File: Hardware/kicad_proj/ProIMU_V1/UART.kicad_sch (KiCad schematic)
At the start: 5 parts

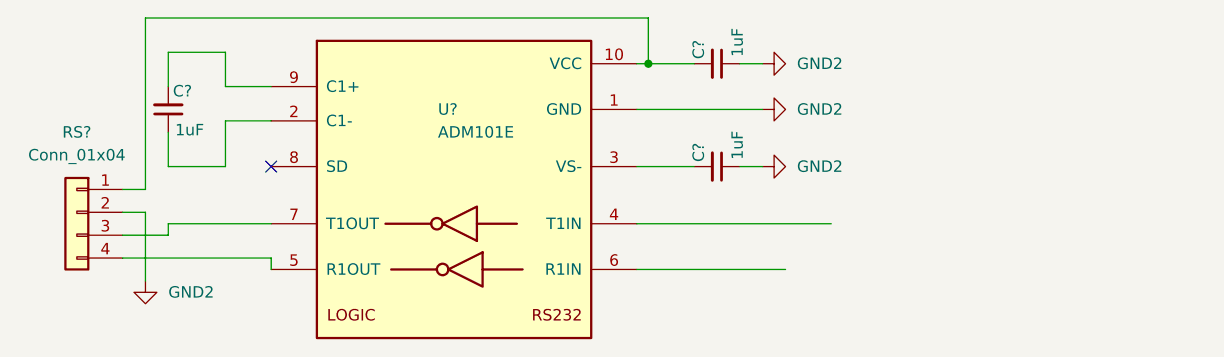
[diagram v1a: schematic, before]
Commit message: Updated schematic and removed redundant schematic
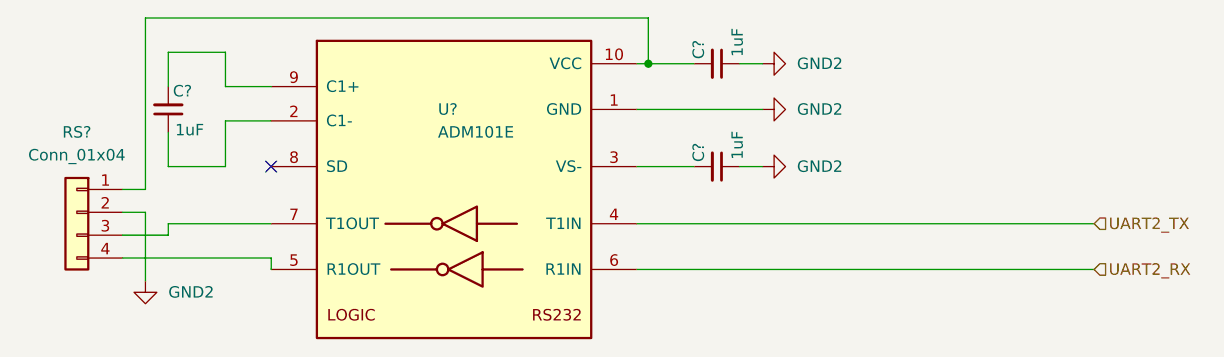
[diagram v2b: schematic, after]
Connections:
- net UART2_TX: now reaches U?.4 (T1IN)
- net UART2_RX: now reaches U?.6 (R1IN)
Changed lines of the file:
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@@
     (stroke (width 0) (type default) (color 0 0 0 0))
   )
-  (wire (pts (xy 168.91 99.06) (xy 190.5 99.06))
+  (wire (pts (xy 168.91 99.06) (xy 219.71 99.06))
     (stroke (width 0) (type default) (color 0 0 0 0))
   )
@@
     (stroke (width 0) (type default) (color 0 0 0 0))
   )
-  (wire (pts (xy 168.91 104.14) (xy 185.42 104.14))
+  (wire (pts (xy 168.91 104.14) (xy 219.71 104.14))
     (stroke (width 0) (type default) (color 0 0 0 0))
   )
@@
     (stroke (width 0) (type default) (color 0 0 0 0))
   )
+  (hierarchical_label "UART2_RX" (shape input) (at 219.71 104.14 0)
+    (effects (font (size 1.27 1.27)) (justify left))
+  )
+  (hierarchical_label "UART2_TX" (shape input) (at 219.71 99.06 0)
+    (effects (font (size 1.27 1.27)) (justify left))
+  )
   (symbol (lib_id "power:GND2") (at 182.88 86.36 90) (unit 1)

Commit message: Updated Schematic and Layout
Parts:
- gave numbers to parts that had none: 5
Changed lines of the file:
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@@
   (symbol (lib_id "power:GND2") (at 182.88 86.36 90) (unit 1)
     (in_bom yes) (on_board yes) (fields_autoplaced)
-    (property "Reference" "#PWR?" (id 0) (at 189.23 86.36 0)
+    (property "Reference" "#PWR0119" (id 0) (at 189.23 86.36 0)
       (effects (font (size 1.27 1.27)) hide)
     )
@@
   (symbol (lib_id "Device:C_Small") (at 177.8 81.28 270) (unit 1)
     (in_bom yes) (on_board yes)
-    (property "Reference" "C?" (id 0) (at 175.768 80.772 0)
+    (property "Reference" "C7" (id 0) (at 175.768 80.772 0)
       (effects (font (size 1.27 1.27)) (justify right))
     )
@@
   (symbol (lib_id "Device:C_Small") (at 116.84 86.36 180) (unit 1)
     (in_bom yes) (on_board yes)
-    (property "Reference" "C?" (id 0) (at 117.348 84.328 0)
+    (property "Reference" "C6" (id 0) (at 117.348 84.328 0)
       (effects (font (size 1.27 1.27)) (justify right))
     )
@@
   (symbol (lib_id "Connector_Generic:Conn_01x04") (at 106.68 97.79 0) (mirror y) (unit 1)
     (in_bom yes) (on_board yes) (fields_autoplaced)
-    (property "Reference" "RS?" (id 0) (at 106.68 88.9 0))
+    (property "Reference" "RS1" (id 0) (at 106.68 88.9 0))
     (property "Value" "Conn_01x04" (id 1) (at 106.68 91.44 0))
     (property "Footprint" "Connector_JST:JST_PH_S4B-PH-SM4-TB_1x04-1MP_P2.00mm_Horizontal" (id 2) (at 106.68 97.79 0)
@@
   (symbol (lib_id "power:GND2") (at 182.88 92.71 90) (unit 1)
     (in_bom yes) (on_board yes) (fields_autoplaced)
-    (property "Reference" "#PWR?" (id 0) (at 189.23 92.71 0)
+    (property "Reference" "#PWR0117" (id 0) (at 189.23 92.71 0)
       (effects (font (size 1.27 1.27)) hide)
     )
@@
   (symbol (lib_id "power:GND2") (at 182.88 81.28 90) (unit 1)
     (in_bom yes) (on_board yes) (fields_autoplaced)
-    (property "Reference" "#PWR?" (id 0) (at 189.23 81.28 0)
+    (property "Reference" "#PWR0118" (id 0) (at 189.23 81.28 0)
       (effects (font (size 1.27 1.27)) hide)
     )
@@
   (symbol (lib_id "Device:C_Small") (at 177.8 92.71 270) (unit 1)
     (in_bom yes) (on_board yes)
-    (property "Reference" "C?" (id 0) (at 175.768 92.202 0)
+    (property "Reference" "C8" (id 0) (at 175.768 92.202 0)
       (effects (font (size 1.27 1.27)) (justify right))
     )
@@
   (symbol (lib_id "power:GND2") (at 114.3 105.41 0) (unit 1)
     (in_bom yes) (on_board yes) (fields_autoplaced)
-    (property "Reference" "#PWR?" (id 0) (at 114.3 111.76 0)
+    (property "Reference" "#PWR0120" (id 0) (at 114.3 111.76 0)
       (effects (font (size 1.27 1.27)) hide)
     )
@@
   (symbol (lib_id "Interface_UART:ADM101E") (at 148.59 86.36 0) (unit 1)
     (in_bom yes) (on_board yes) (fields_autoplaced)
-    (property "Reference" "U?" (id 0) (at 146.7994 86.36 0)
+    (property "Reference" "U2" (id 0) (at 146.7994 86.36 0)
       (effects (font (size 1.27 1.27)) (justify left))
     )
